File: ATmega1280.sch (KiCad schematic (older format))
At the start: 25 parts, among them CON1 AVR-ISP-10, IC1 ATMEGA1280-A, P1 CONN_02X20, SW1 SW_PUSH, U1 74HCT541_PWR, U5 CONN3, X1 CRYSTAL

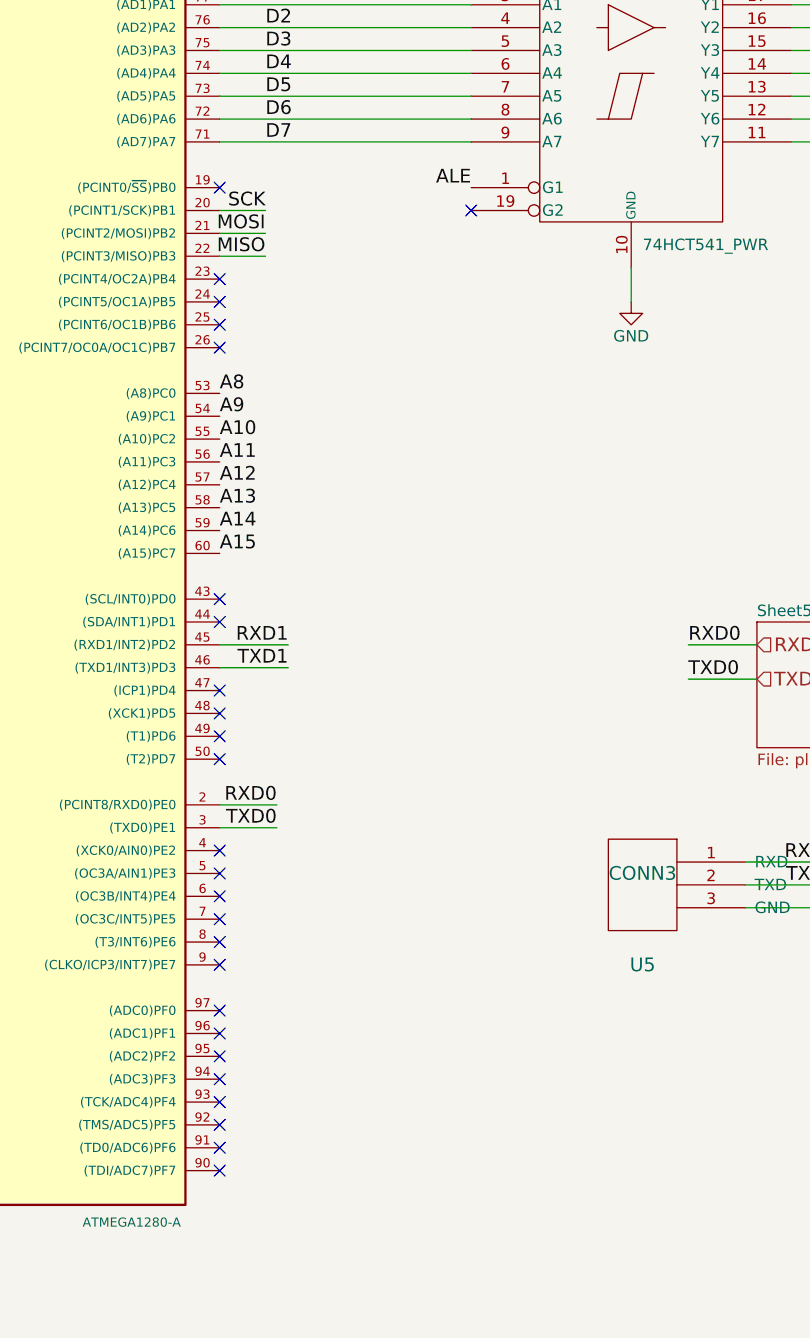
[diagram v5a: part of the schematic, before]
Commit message: Добавлен JTAG и SPI
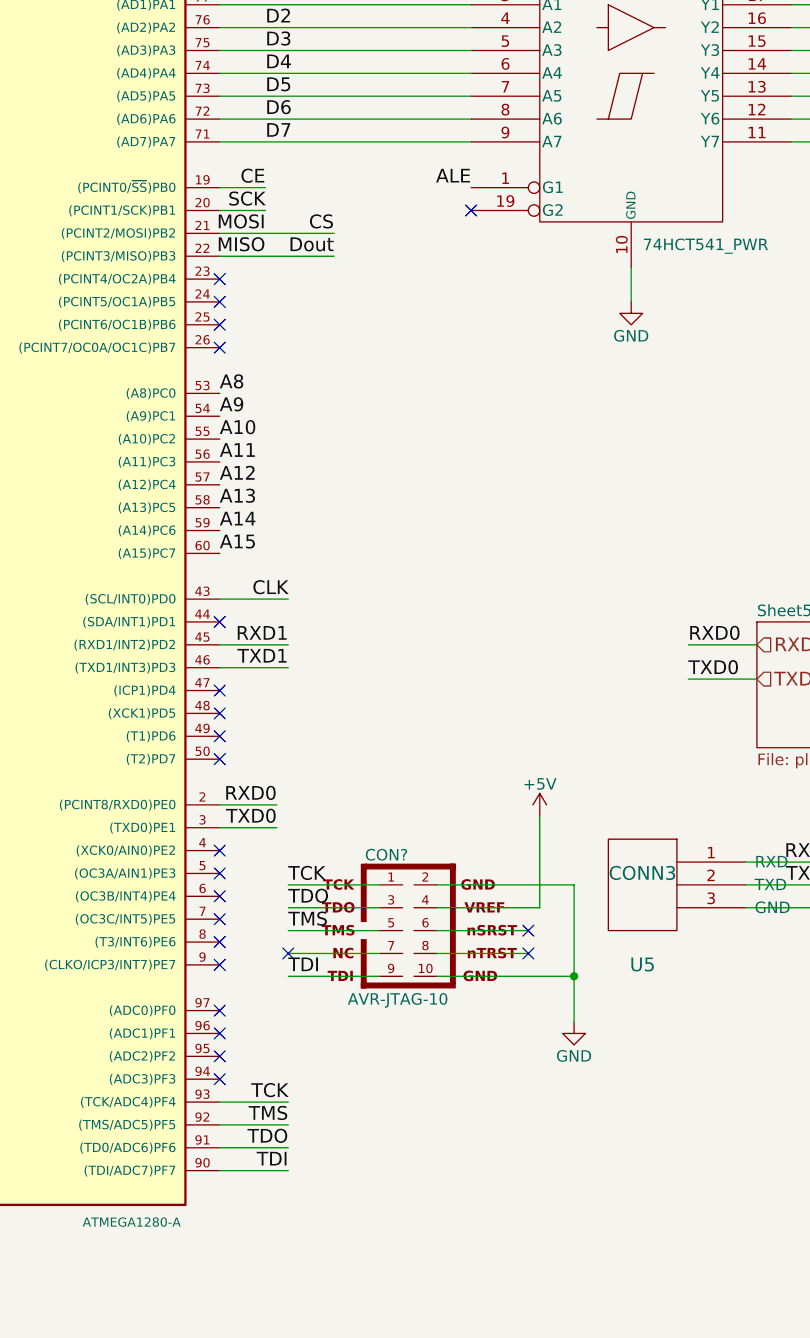
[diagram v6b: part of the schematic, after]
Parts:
- added CON?: AVR-JTAG-10, AVR-JTAG-10, symbol AVR-JTAG-10
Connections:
- net MISO is gone; now on net Dout: CON1.9, IC1.22 ((PCINT3/MISO)PB3)
- net MOSI is gone; now on net CS: CON1.1, IC1.21 ((PCINT2/MOSI)PB2)
- net +5V: now also CON?.4
- net CE: now also IC1.19 ((PCINT0/~SS~)PB0)
- net CLK: now also IC1.43 ((SCL/INT0)PD0)
- net GND: now also CON?.10, CON?.2
- net TDI: now reaches IC1.90 ((TDI/ADC7)PF7)
- net TDI: now also CON?.9
- net TDO: now reaches IC1.91 ((TD0/ADC6)PF6)
- net TDO: now also CON?.3
- net TMS: now reaches IC1.92 ((TMS/ADC5)PF5)
- net TMS: now also CON?.5
- net TCK: now reaches IC1.93 ((TCK/ADC4)PF4)
- net TCK: now also CON?.1
- no-connect marks 59 -> 56
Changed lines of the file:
@@
 NoConn ~ 3150 6650
 NoConn ~ 3150 6750
-NoConn ~ 5750 6950
-NoConn ~ 5750 6850
-NoConn ~ 5750 6750
-NoConn ~ 5750 6650
 NoConn ~ 5750 6550
 NoConn ~ 5750 6450
@@
 NoConn ~ 5750 4950
 NoConn ~ 5750 4850
-NoConn ~ 5750 4450
 NoConn ~ 5750 3350
 NoConn ~ 5750 3250
 NoConn ~ 5750 3150
 NoConn ~ 5750 3050
-NoConn ~ 5750 2650
 Text Label 6000 5350 2    60   ~ 0
 RXD0
@@
 Connection ~ 10150 3350
 Wire Wire Line
-	5750 2950 5950 2950
-Wire Wire Line
-	5750 2850 5950 2850
+	5750 2950 6250 2950
+Wire Wire Line
+	5750 2850 6250 2850
 Wire Wire Line
 	5750 2750 5950 2750
@@
 	1    0    0    -1
 $EndComp
+Wire Wire Line
+	5750 4450 6050 4450
+Text Label 6050 4450 2    60   ~ 0
+CLK
+Wire Wire Line
+	5750 2650 5950 2650
+Text Label 5950 2650 2    60   ~ 0
+CE
+Text Label 6250 2950 2    60   ~ 0
+Dout
+Text Label 6250 2850 2    60   ~ 0
+CS
+$Comp
+L AVR-JTAG-10 CON?
+U 1 1 57211968
+P 6650 5900
+F 0 "CON?" H 6480 6230 50  0000 C CNN
+F 1 "AVR-JTAG-10" H 6310 5570 50  0000 L BNN
+F 2 "AVR-JTAG-10" V 6080 5920 50  0001 C CNN
+F 3 "" H 6650 5900 50  0000 C CNN
+	1    6650 5900
+	1    0    0    -1
+$EndComp
+Wire Wire Line
+	5750 6650 6050 6650
+Wire Wire Line
+	5750 6750 6050 6750
+Wire Wire Line
+	5750 6850 6050 6850
+Wire Wire Line
+	5750 6950 6050 6950
+Wire Wire Line
+	6450 5700 6050 5700
+Wire Wire Line
+	6450 5800 6050 5800
+Wire Wire Line
+	6450 5900 6050 5900
+Wire Wire Line
+	6450 6000 6050 6000
+Wire Wire Line
+	6450 6100 6050 6100
+NoConn ~ 6050 6000
+Text Label 6050 5700 0    60   ~ 0
+TCK
+Text Label 6050 5800 0    60   ~ 0
+TDO
+Text Label 6050 5900 0    60   ~ 0
+TMS
+Text Label 6050 6100 0    60   ~ 0
+TDI
+Text Label 6050 6650 2    60   ~ 0
+TCK
+Text Label 6050 6750 2    60   ~ 0
+TMS
+Text Label 6050 6850 2    60   ~ 0
+TDO
+Text Label 6050 6950 2    60   ~ 0
+TDI
+Wire Wire Line
+	6700 5900 7100 5900
+Wire Wire Line
+	6700 6000 7100 6000
+NoConn ~ 7100 5900
+NoConn ~ 7100 6000
+Wire Wire Line
+	6700 5700 7300 5700
+Wire Wire Line
+	7300 5700 7300 6300
+Wire Wire Line
+	6700 6100 7300 6100
+Connection ~ 7300 6100
+$Comp
+L GND #PWR?
+U 1 1 57212B56
+P 7300 6300
+F 0 "#PWR?" H 7300 6050 50  0001 C CNN
+F 1 "GND" H 7300 6150 50  0000 C CNN
+F 2 "" H 7300 6300 50  0000 C CNN
+F 3 "" H 7300 6300 50  0000 C CNN
+	1    7300 6300
+	1    0    0    -1
+$EndComp
+Wire Wire Line
+	6700 5800 7150 5800
+Wire Wire Line
+	7150 5800 7150 5400
+$Comp
+L +5V #PWR?
+U 1 1 57212CB0
+P 7150 5400
+F 0 "#PWR?" H 7150 5250 50  0001 C CNN
+F 1 "+5V" H 7150 5540 50  0000 C CNN
+F 2 "" H 7150 5400 50  0000 C CNN
+F 3 "" H 7150 5400 50  0000 C CNN
+	1    7150 5400
+	1    0    0    -1
+$EndComp

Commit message: Изменения в CvPCB
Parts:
- C10, C11, C12, C9: footprint (none) -> Capacitors_SMD:C_0402
- C13, C7, C8: renamed from C?; footprint (none) -> Capacitors_SMD:C_0603_HandSoldering
- C21, C22: footprint (none) -> Capacitors_SMD:C_0603_HandSoldering
- CON2: renamed from CON?; footprint AVR-JTAG-10 -> Pin_Headers:Pin_Header_Straight_2x05
- IC1: footprint TQFP100 -> Housings_QFP:TQFP-100_14x14mm_Pitch0.5mm
- JP1: footprint (none) -> Connect:PINHEAD1-2
- P1: footprint (none) -> Connect:IDC_Header_Straight_40pins
- R10, R11, R9: renamed from R?; footprint (none) -> Resistors_SMD:R_0402
- R6: footprint (none) -> Resistors_SMD:R_0402
- SW1: footprint (none) -> Buttons_Switches_ThroughHole:SW_DIP_x1_Slide
- U1: footprint (none) -> Display:HDSP-48xx
- U5: footprint (none) -> Connect:Wafer_Horizontal10x5.8x7RM2.5-3
- U6, U7, U8: renamed from U?; footprint (none) -> Connectors_Molex:Connector_Microfit3_Header_02x03_Straight_43045-0628
- U9: renamed from U?; footprint (none) -> Connect:Wafer_Vertical10x5.8x7RM2.5-3
- X1: footprint (none) -> Crystals:Crystal_FOX-FE_SMD

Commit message: Небольшие изменения
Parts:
- removed R10, R11, R9: 150, Resistors_SMD:R_0402, symbol R
- C13, C7, C8: value 104 -> 10nF
- SW1: footprint Buttons_Switches_ThroughHole:SW_DIP_x1_Slide -> Buttons_Switches_ThroughHole:SW_PUSH_SMALL
- U9: footprint Connect:Wafer_Vertical10x5.8x7RM2.5-3 -> Pin_Headers:Pin_Header_Angled_1x03
- X1: footprint Crystals:Crystal_FOX-FE_SMD -> Crystals:Crystal_HC49-U_Vertical
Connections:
- net +5V: now also C13.1, C7.1, C8.1, U6.3 (Vcc), U7.3 (Vcc), U8.3 (Vcc)
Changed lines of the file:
@@
 F 0 "X1" H 2300 2800 50  0000 C CNN
 F 1 "CRYSTAL" H 2300 2500 50  0000 C CNN
-F 2 "Crystals:Crystal_FOX-FE_SMD" H 2300 2650 50  0001 C CNN
+F 2 "Crystals:Crystal_HC49-U_Vertical" H 2300 2650 50  0001 C CNN
 F 3 "" H 2300 2650 50  0000 C CNN
 	1    2300 2650
@@
 F 0 "SW1" H 2300 1860 50  0000 C CNN
 F 1 "SW_PUSH" H 2150 1670 50  0000 C CNN
-F 2 "Buttons_Switches_ThroughHole:SW_DIP_x1_Slide" H 2150 1750 50  0001 C CNN
+F 2 "Buttons_Switches_ThroughHole:SW_PUSH_SMALL" H 2150 1750 50  0001 C CNN
 F 3 "" H 2150 1750 50  0000 C CNN
 	1    2150 1750
@@
 F 0 "U9" H 9600 4750 60  0000 C CNN
 F 1 "CONN3" H 9600 5150 60  0000 C CNN
-F 2 "Connect:Wafer_Vertical10x5.8x7RM2.5-3" H 9250 5400 60  0001 C CNN
+F 2 "Pin_Headers:Pin_Header_Angled_1x03" H 9250 5400 60  0001 C CNN
 F 3 "" H 9250 5400 60  0000 C CNN
 	1    9250 5400
@@
 $EndComp
 $Comp
-L R R10
-U 1 1 571E9453
-P 1350 4000
-F 0 "R10" V 1430 4000 50  0000 C CNN
-F 1 "150" V 1350 4000 50  0000 C CNN
-F 2 "Resistors_SMD:R_0402" V 1280 4000 50  0001 C CNN
-F 3 "" H 1350 4000 50  0000 C CNN
-	1    1350 4000
-	0    1    1    0
-$EndComp
-$Comp
 L C C7
 U 1 1 571E94CF
 P 1650 4150
 F 0 "C7" H 1675 4250 50  0000 L CNN
-F 1 "104" H 1675 4050 50  0000 L CNN
+F 1 "10nF" H 1675 4050 50  0000 L CNN
 F 2 "Capacitors_SMD:C_0603_HandSoldering" H 1688 4000 50  0001 C CNN
 F 3 "" H 1650 4150 50  0000 C CNN
@@
 	800  4450 800  4000
 Wire Wire Line
-	800  4000 1200 4000
+	800  4000 2000 4000
 Wire Wire Line
 	1050 4000 1050 3900
@@
 	1    0    0    -1
 $EndComp
-Wire Wire Line
-	1500 4000 2000 4000
 Connection ~ 2000 4150
 Wire Wire Line
@@
 	2100 6800 2100 7150
 $Comp
-L R R9
-U 1 1 571EBFEE
-P 1250 5000
-F 0 "R9" V 1330 5000 50  0000 C CNN
-F 1 "150" V 1250 5000 50  0000 C CNN
-F 2 "Resistors_SMD:R_0402" V 1180 5000 50  0001 C CNN
-F 3 "" H 1250 5000 50  0000 C CNN
-	1    1250 5000
-	0    1    1    0
-$EndComp
-$Comp
-L R R11
-U 1 1 571EC096
-P 1350 6150
-F 0 "R11" V 1430 6150 50  0000 C CNN
-F 1 "150" V 1350 6150 50  0000 C CNN
-F 2 "Resistors_SMD:R_0402" V 1280 6150 50  0001 C CNN
-F 3 "" H 1350 6150 50  0000 C CNN
-	1    1350 6150
-	0    1    1    0
-$EndComp
-$Comp
 L C C8
 U 1 1 571EC15B
 P 1700 5150
 F 0 "C8" H 1725 5250 50  0000 L CNN
-F 1 "104" H 1725 5050 50  0000 L CNN
+F 1 "10nF" H 1725 5050 50  0000 L CNN
 F 2 "Capacitors_SMD:C_0603_HandSoldering" H 1738 5000 50  0001 C CNN
 F 3 "" H 1700 5150 50  0000 C CNN
@@
 P 1750 6350
 F 0 "C13" H 1775 6450 50  0000 L CNN
-F 1 "104" H 1775 6250 50  0000 L CNN
+F 1 "10nF" H 1775 6250 50  0000 L CNN
 F 2 "Capacitors_SMD:C_0603_HandSoldering" H 1788 6200 50  0001 C CNN
 F 3 "" H 1750 6350 50  0000 C CNN
@@
 $EndComp
 Wire Wire Line
-	1400 5000 1950 5000
+	800  5000 1950 5000
 Wire Wire Line
 	1950 5000 1950 5400
@@
 Connection ~ 650  5150
 Wire Wire Line
-	800  5000 1100 5000
-Wire Wire Line
 	950  5000 950  4900
 Wire Wire Line
@@
 	1000 6000 1000 6150
 Wire Wire Line
-	850  6150 1200 6150
+	850  6150 2000 6150
 Wire Wire Line
 	850  6150 850  6700
@@
 Wire Wire Line
 	2000 6350 1900 6350
-Wire Wire Line
-	1500 6150 2000 6150
 Connection ~ 2000 6350
 Wire Wire Line
